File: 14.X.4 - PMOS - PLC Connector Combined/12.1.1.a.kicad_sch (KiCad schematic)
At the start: 30 parts, among them J201 Conn_01x01_PAD, J202 Conn_01x01_PAD, J203 Conn_01x01_PAD, J204 Conn_01x01_PAD, J205 Conn_01x01_PAD, J206 Conn_01x01_PAD, J207 Conn_01x01_PAD, J208 Conn_01x01_PAD, J209 Conn_01x01_PAD, J210 Conn_01x01_PAD, J211 Conn_01x01_PAD, J212 Conn_01x01_PAD, J213 Conn_01x01_PAD, J214 Conn_01x01_PAD, J215 Conn_01x01_PAD, J216 Conn_01x01_PAD, J217 Conn_01x01_PAD, J218 Conn_01x01_PAD, J219 Conn_01x01_PAD, J220 Conn_01x01_PAD, J221 Dorabo-DB128L_5_08_2P_BKS, J222 Dorabo-DB128L_5_08_2P_BKS, J223 Dorabo-DB128L_5_08_2P_BKS, J224 Dorabo-DB128L_5_08_2P_BKS, J225 Dorabo-DB128L_5_08_2P_BKS, J226 B04B-XASK-1

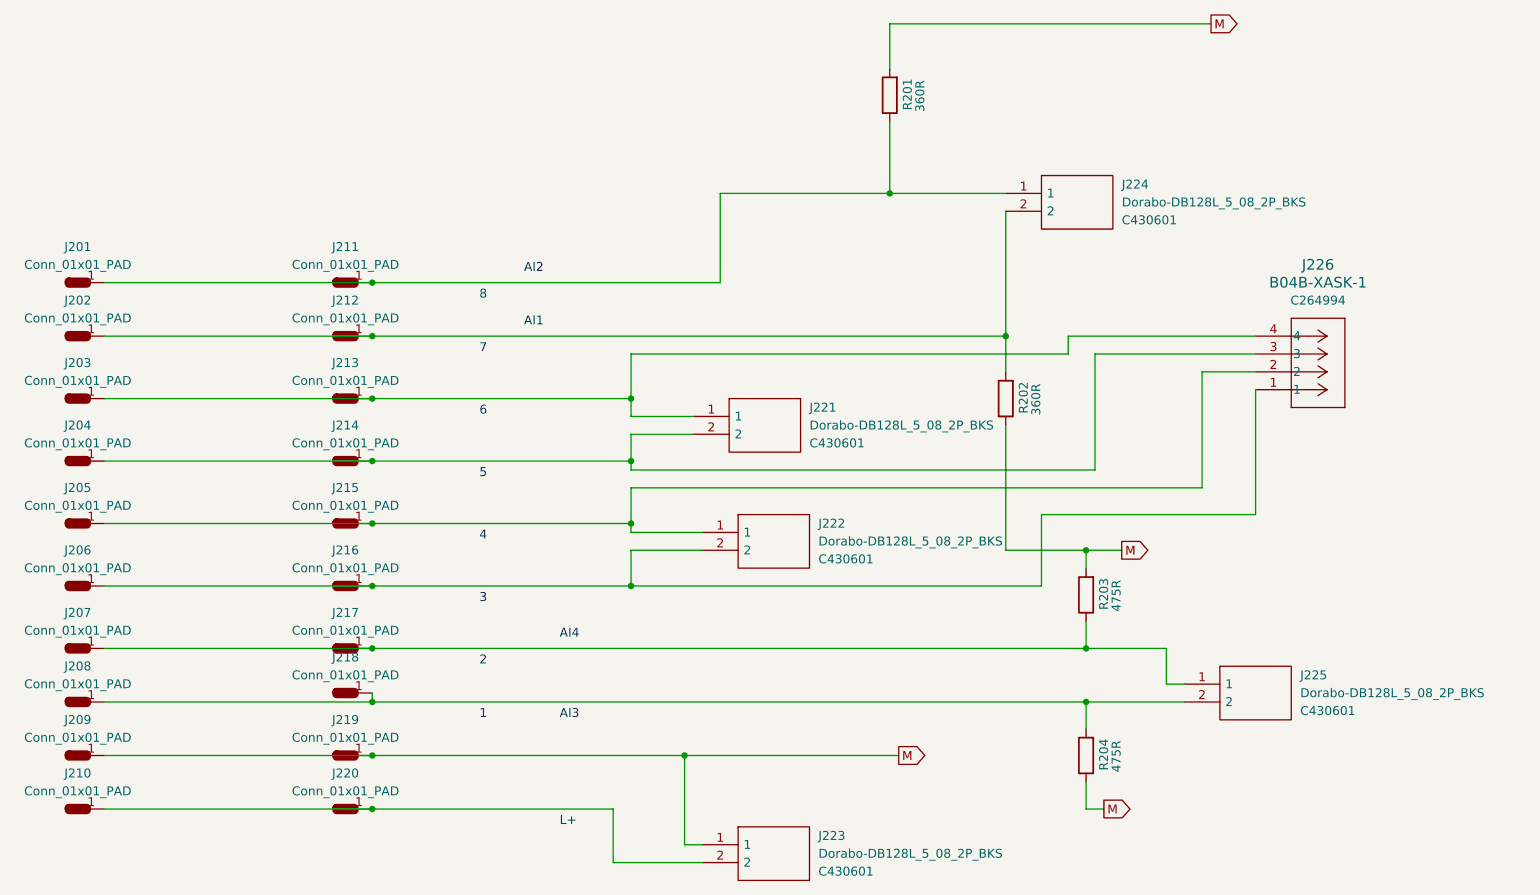
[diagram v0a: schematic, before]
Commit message: orientation of U1,U2,U3 and U4
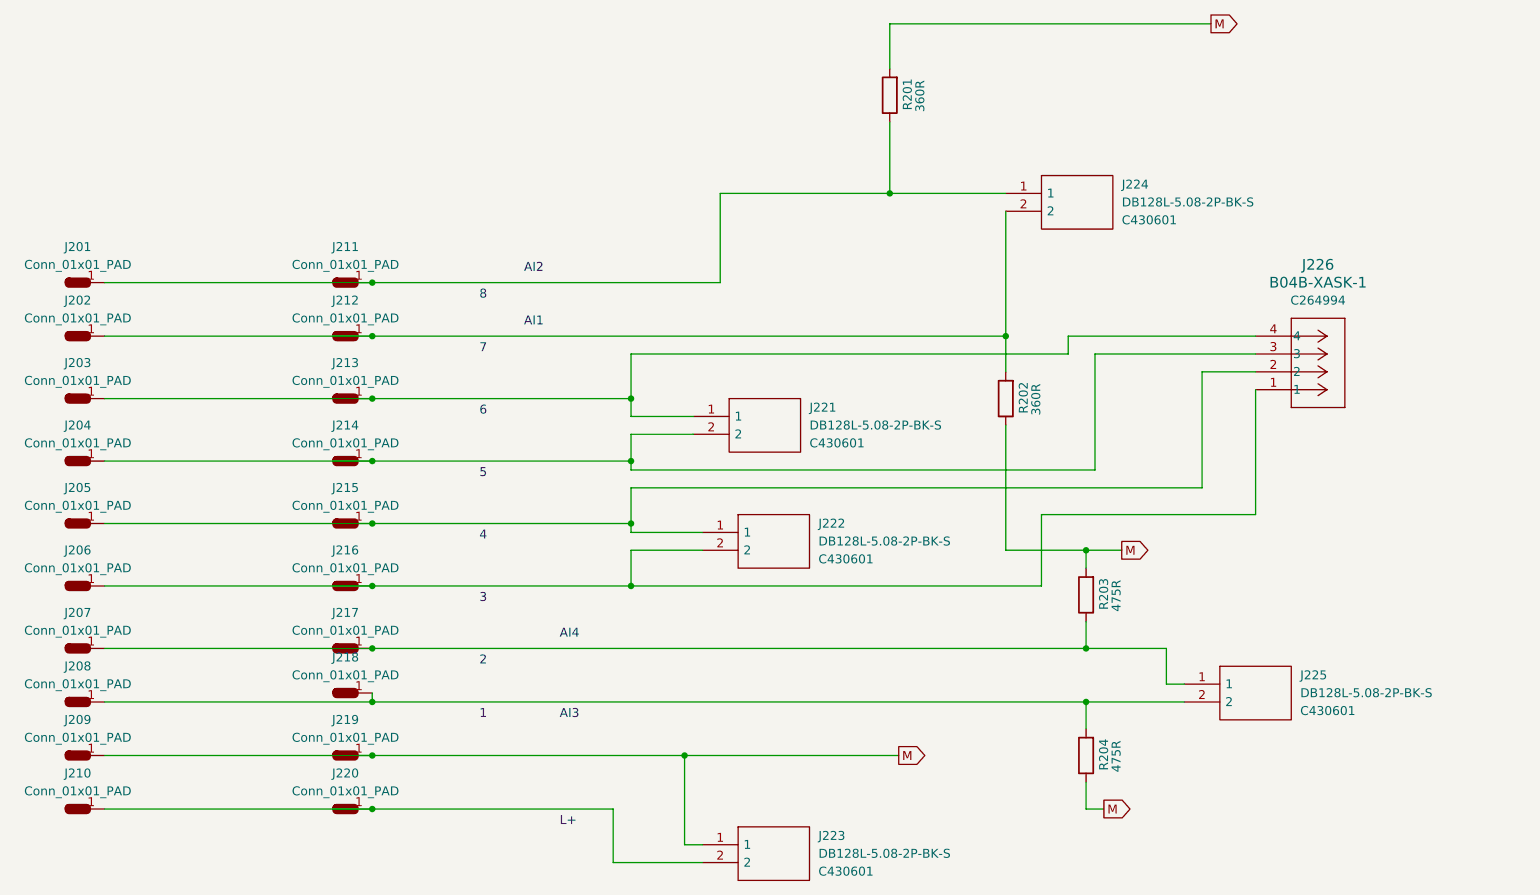
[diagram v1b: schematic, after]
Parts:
- J221, J222, J223, J224, J225: value Dorabo-DB128L_5_08_2P_BKS -> DB128L-5.08-2P-BK-S
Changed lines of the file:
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@@
       (effects (font (size 1.27 1.27)) (justify left))
     )
-    (property "Value" "Dorabo-DB128L_5_08_2P_BKS" (at 226.06 128.27 0)
+    (property "Value" "DB128L-5.08-2P-BK-S" (at 226.06 128.27 0)
       (effects (font (size 1.27 1.27)) (justify left))
     )
@@
       (effects (font (size 1.27 1.27)) (justify left))
     )
-    (property "Value" "Dorabo-DB128L_5_08_2P_BKS" (at 157.48 151.13 0)
+    (property "Value" "DB128L-5.08-2P-BK-S" (at 157.48 151.13 0)
       (effects (font (size 1.27 1.27)) (justify left))
     )
@@
       (effects (font (size 1.27 1.27)) (justify left))
     )
-    (property "Value" "Dorabo-DB128L_5_08_2P_BKS" (at 157.48 106.68 0)
+    (property "Value" "DB128L-5.08-2P-BK-S" (at 157.48 106.68 0)
       (effects (font (size 1.27 1.27)) (justify left))
     )
@@
       (effects (font (size 1.27 1.27)) (justify left))
     )
-    (property "Value" "Dorabo-DB128L_5_08_2P_BKS" (at 200.66 58.42 0)
+    (property "Value" "DB128L-5.08-2P-BK-S" (at 200.66 58.42 0)
       (effects (font (size 1.27 1.27)) (justify left))
     )
@@
       (effects (font (size 1.27 1.27)) (justify left))
     )
-    (property "Value" "Dorabo-DB128L_5_08_2P_BKS" (at 156.21 90.17 0)
-      (effects (font (size 1.27 1.27)) (justify left))
-    )
+    (property "Value" "DB128L-5.08-2P-BK-S" (at 156.21 90.17 0)
+      (effects (font (size 1.27 1.27)) (justify left))
+    )
